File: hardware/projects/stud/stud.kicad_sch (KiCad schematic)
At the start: 1 part, among them U2 TAC5242

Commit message: add RA8M2, propose memory chip
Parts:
- added IC1: R7KA8M2JFLCAC#UC0, vendor:BGA289C65P17X17_1200X1200X138, symbol vendor:R7KA8M2JFLCAC#UC0
- added U1: IS42VM32160E-75BLI, vendor:TFBGA-90_8X13_ISI, symbol vendor:IS42VM32160E-75BLI
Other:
- moved on the sheet: U2

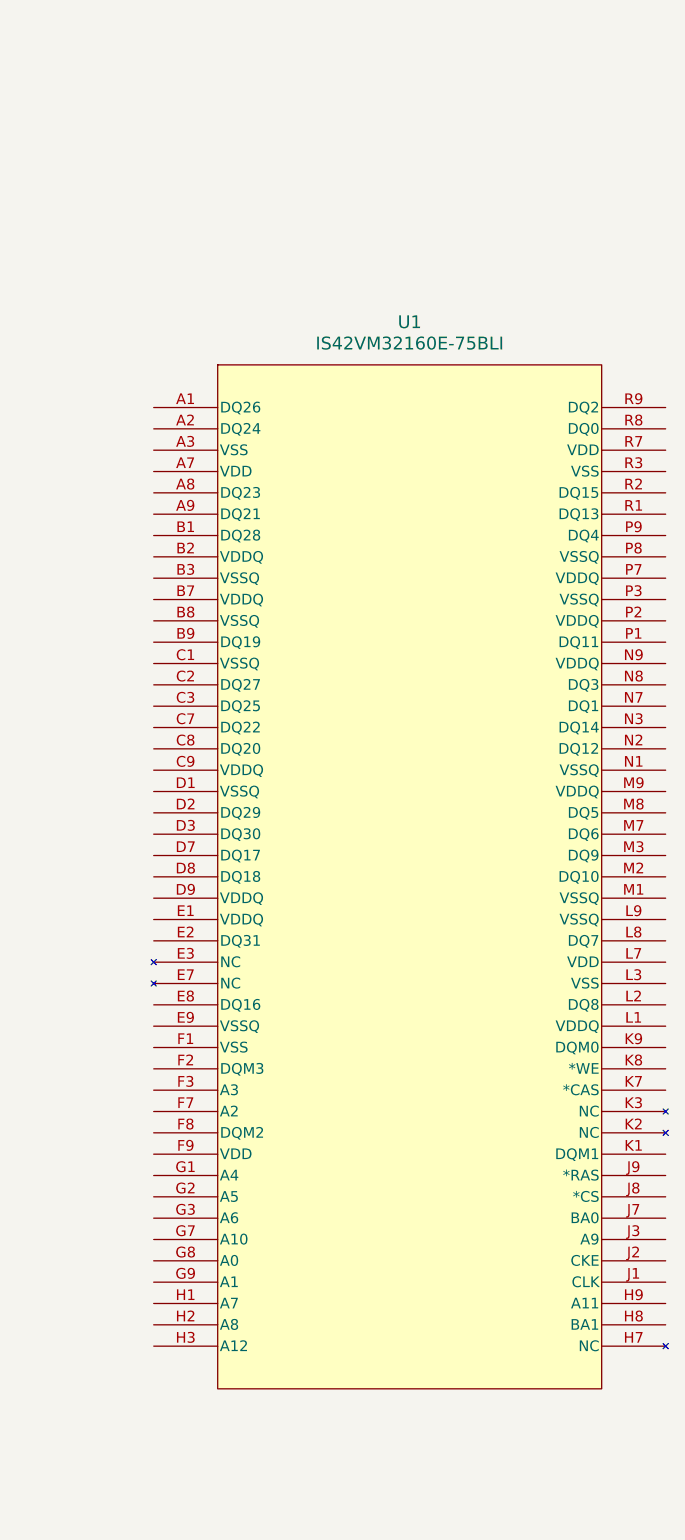
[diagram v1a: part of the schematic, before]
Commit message: switch SDRAM chips at fable's behest
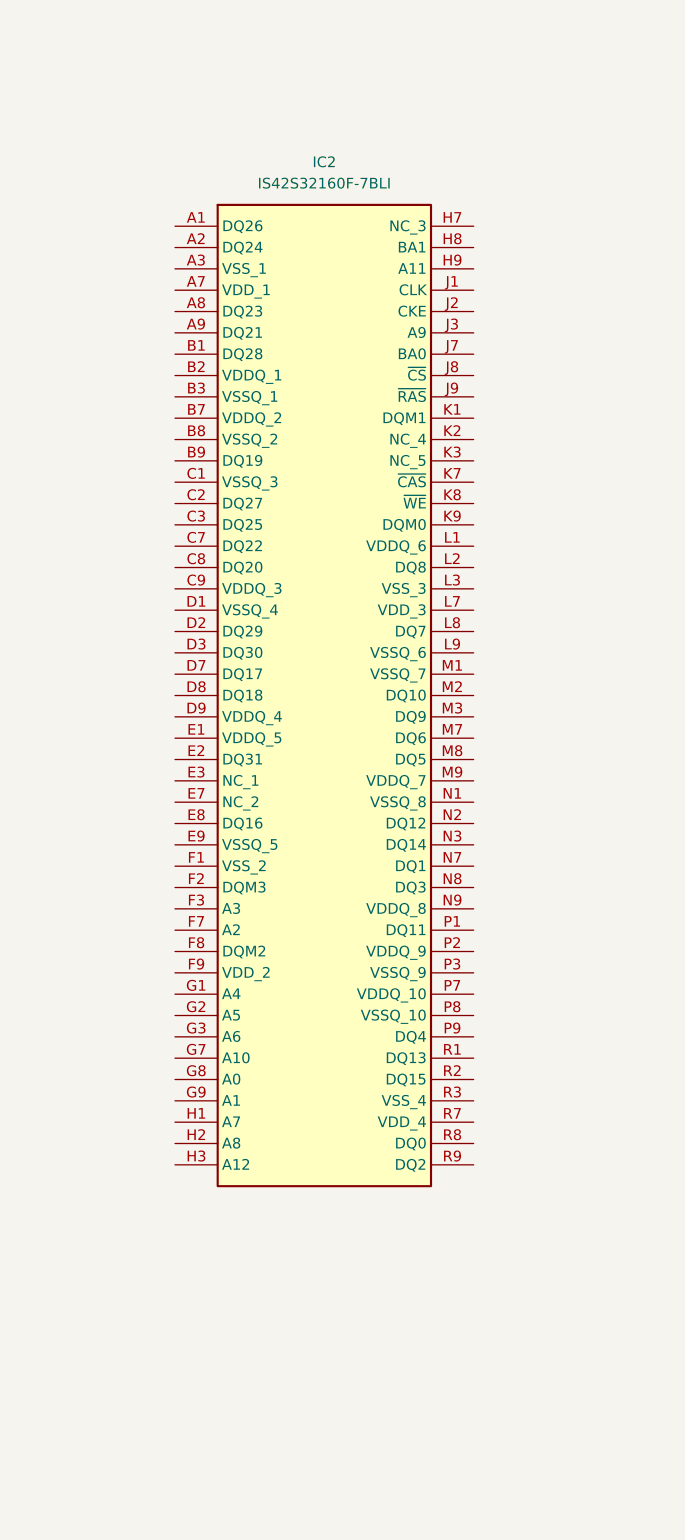
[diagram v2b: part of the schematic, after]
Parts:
- removed U1: IS42VM32160E-75BLI, vendor:TFBGA-90_8X13_ISI, symbol vendor:IS42VM32160E-75BLI
- added IC2: IS42S32160F-7BLI, vendor:BGA90C80P9X15_800X1300X120, symbol vendor:IS42S32160F-7BLI

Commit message: think about routing SDRAM traces
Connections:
- net DQ26: now reaches IC1.L3 (PC04)
- net DQ26: now also IC2.A1 (DQ26)
- net DQ21: now reaches IC1.L4 (PC09)
- net DQ21: now also IC2.A9 (DQ21)
- net DQ25: now reaches IC1.L5 (PC05)
- net DQ25: now also IC2.C3 (DQ25)
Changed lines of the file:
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@@
 		(company "stillmar electric")
+	)
+	(global_label "DQ26"
+		(shape bidirectional)
+		(at 184.15 184.15 180)
+		(fields_autoplaced yes)
+		(effects
+			(font
+				(size 1.27 1.27)
+			)
+			(justify right)
+		)
+		(property "Intersheetrefs" "${INTERSHEET_REFS}"
+			(at 175.034 184.15 0)
+			(hide yes)
+			(show_name no)
+			(do_not_autoplace no)
+			(effects
+				(font
+					(size 1.27 1.27)
+				)
+				(justify right)
+			)
+		)
+	)
+	(global_label "DQ25"
+		(shape bidirectional)
+		(at 107.95 167.64 0)
+		(fields_autoplaced yes)
+		(effects
+			(font
+				(size 1.27 1.27)
+			)
+			(justify left)
+		)
+		(property "Intersheetrefs" "${INTERSHEET_REFS}"
+			(at 117.066 167.64 0)
+			(hide yes)
+			(show_name no)
+			(do_not_autoplace no)
+			(effects
+				(font
+					(size 1.27 1.27)
+				)
+				(justify left)
+			)
+		)
+	)
+	(global_label "DQ25"
+		(shape bidirectional)
+		(at 184.15 219.71 180)
+		(fields_autoplaced yes)
+		(effects
+			(font
+				(size 1.27 1.27)
+			)
+			(justify right)
+		)
+		(property "Intersheetrefs" "${INTERSHEET_REFS}"
+			(at 175.034 219.71 0)
+			(hide yes)
+			(show_name no)
+			(do_not_autoplace no)
+			(effects
+				(font
+					(size 1.27 1.27)
+				)
+				(justify right)
+			)
+		)
+	)
+	(global_label "DQ26"
+		(shape bidirectional)
+		(at 107.95 162.56 0)
+		(fields_autoplaced yes)
+		(effects
+			(font
+				(size 1.27 1.27)
+			)
+			(justify left)
+		)
+		(property "Intersheetrefs" "${INTERSHEET_REFS}"
+			(at 117.066 162.56 0)
+			(hide yes)
+			(show_name no)
+			(do_not_autoplace no)
+			(effects
+				(font
+					(size 1.27 1.27)
+				)
+				(justify left)
+			)
+		)
+	)
+	(global_label "DQ21"
+		(shape bidirectional)
+		(at 184.15 196.85 180)
+		(fields_autoplaced yes)
+		(effects
+			(font
+				(size 1.27 1.27)
+			)
+			(justify right)
+		)
+		(property "Intersheetrefs" "${INTERSHEET_REFS}"
+			(at 175.034 196.85 0)
+			(hide yes)
+			(show_name no)
+			(do_not_autoplace no)
+			(effects
+				(font
+					(size 1.27 1.27)
+				)
+				(justify right)
+			)
+		)
+	)
+	(global_label "DQ21"
+		(shape bidirectional)
+		(at 107.95 165.1 0)
+		(fields_autoplaced yes)
+		(effects
+			(font
+				(size 1.27 1.27)
+			)
+			(justify left)
+		)
+		(property "Intersheetrefs" "${INTERSHEET_REFS}"
+			(at 117.066 165.1 0)
+			(hide yes)
+			(show_name no)
+			(do_not_autoplace no)
+			(effects
+				(font
+					(size 1.27 1.27)
+				)
+				(justify left)
+			)
+		)
 	)
 	(symbol

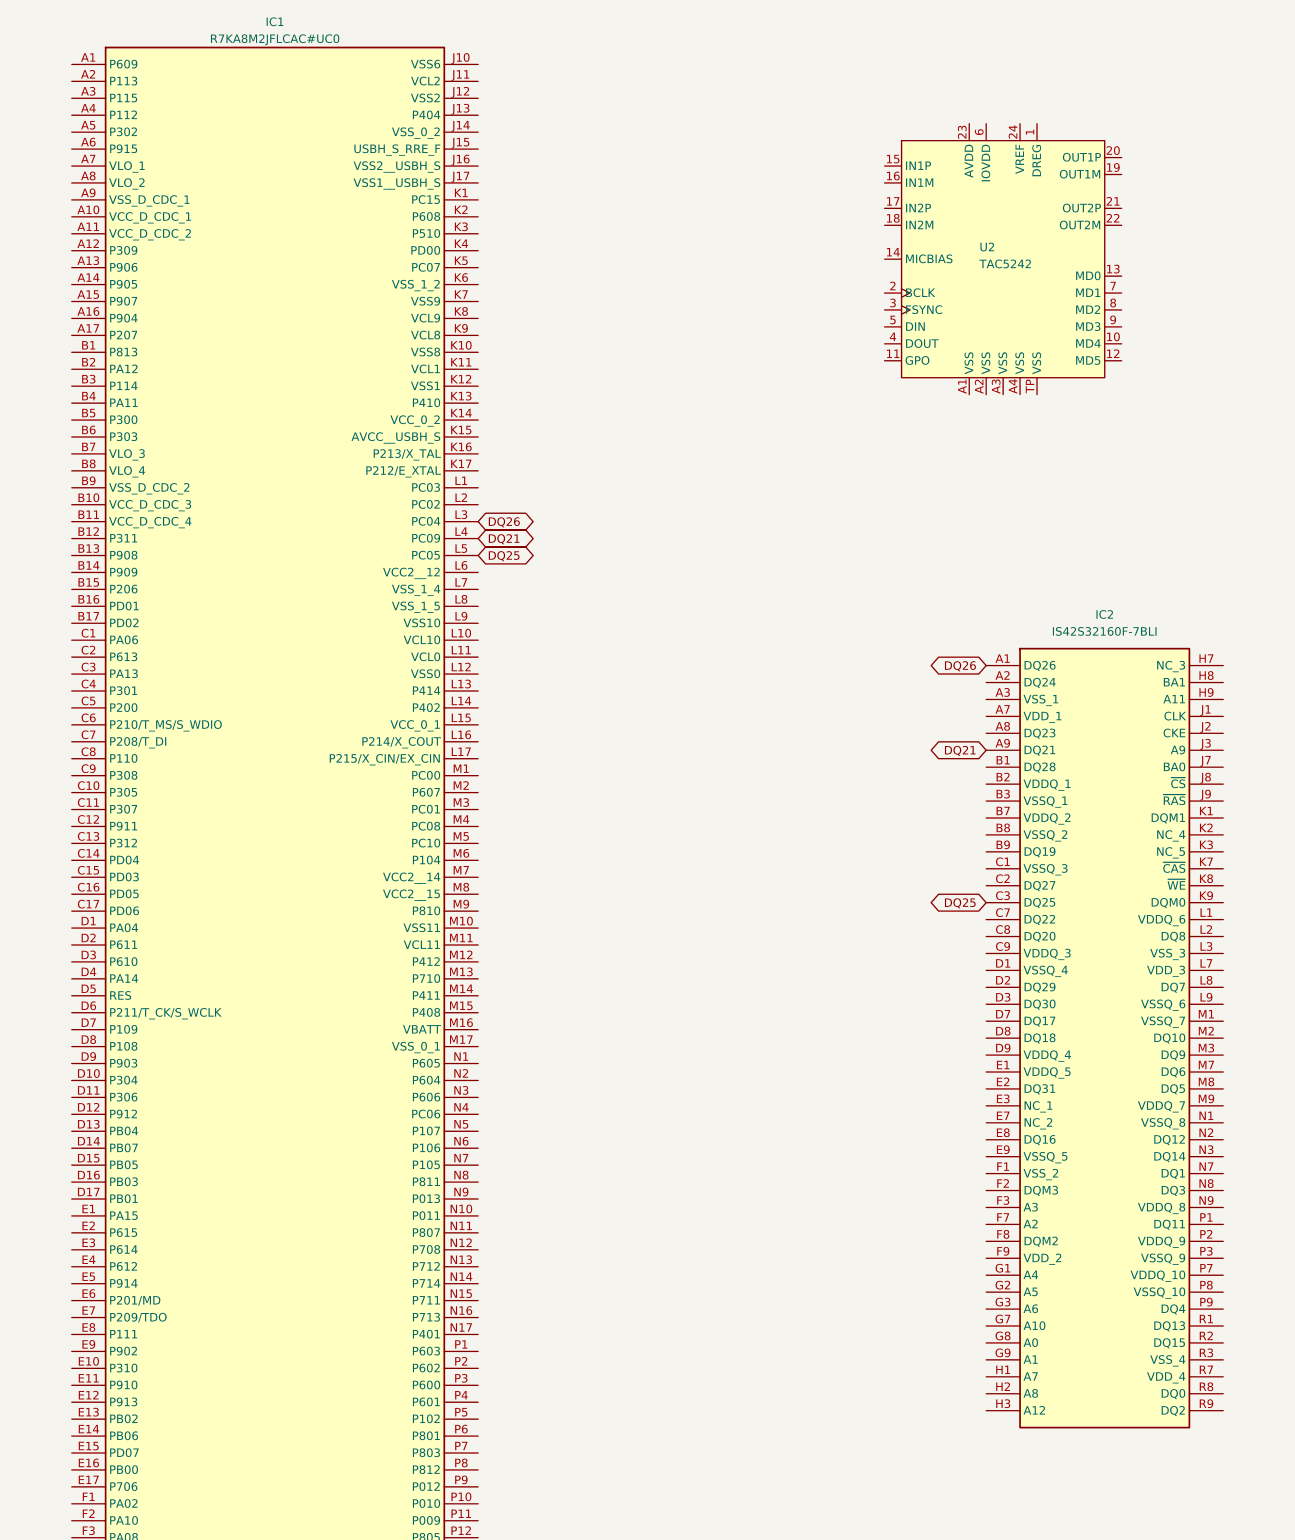
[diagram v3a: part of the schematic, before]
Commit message: add enough DQ nets to peek at connections
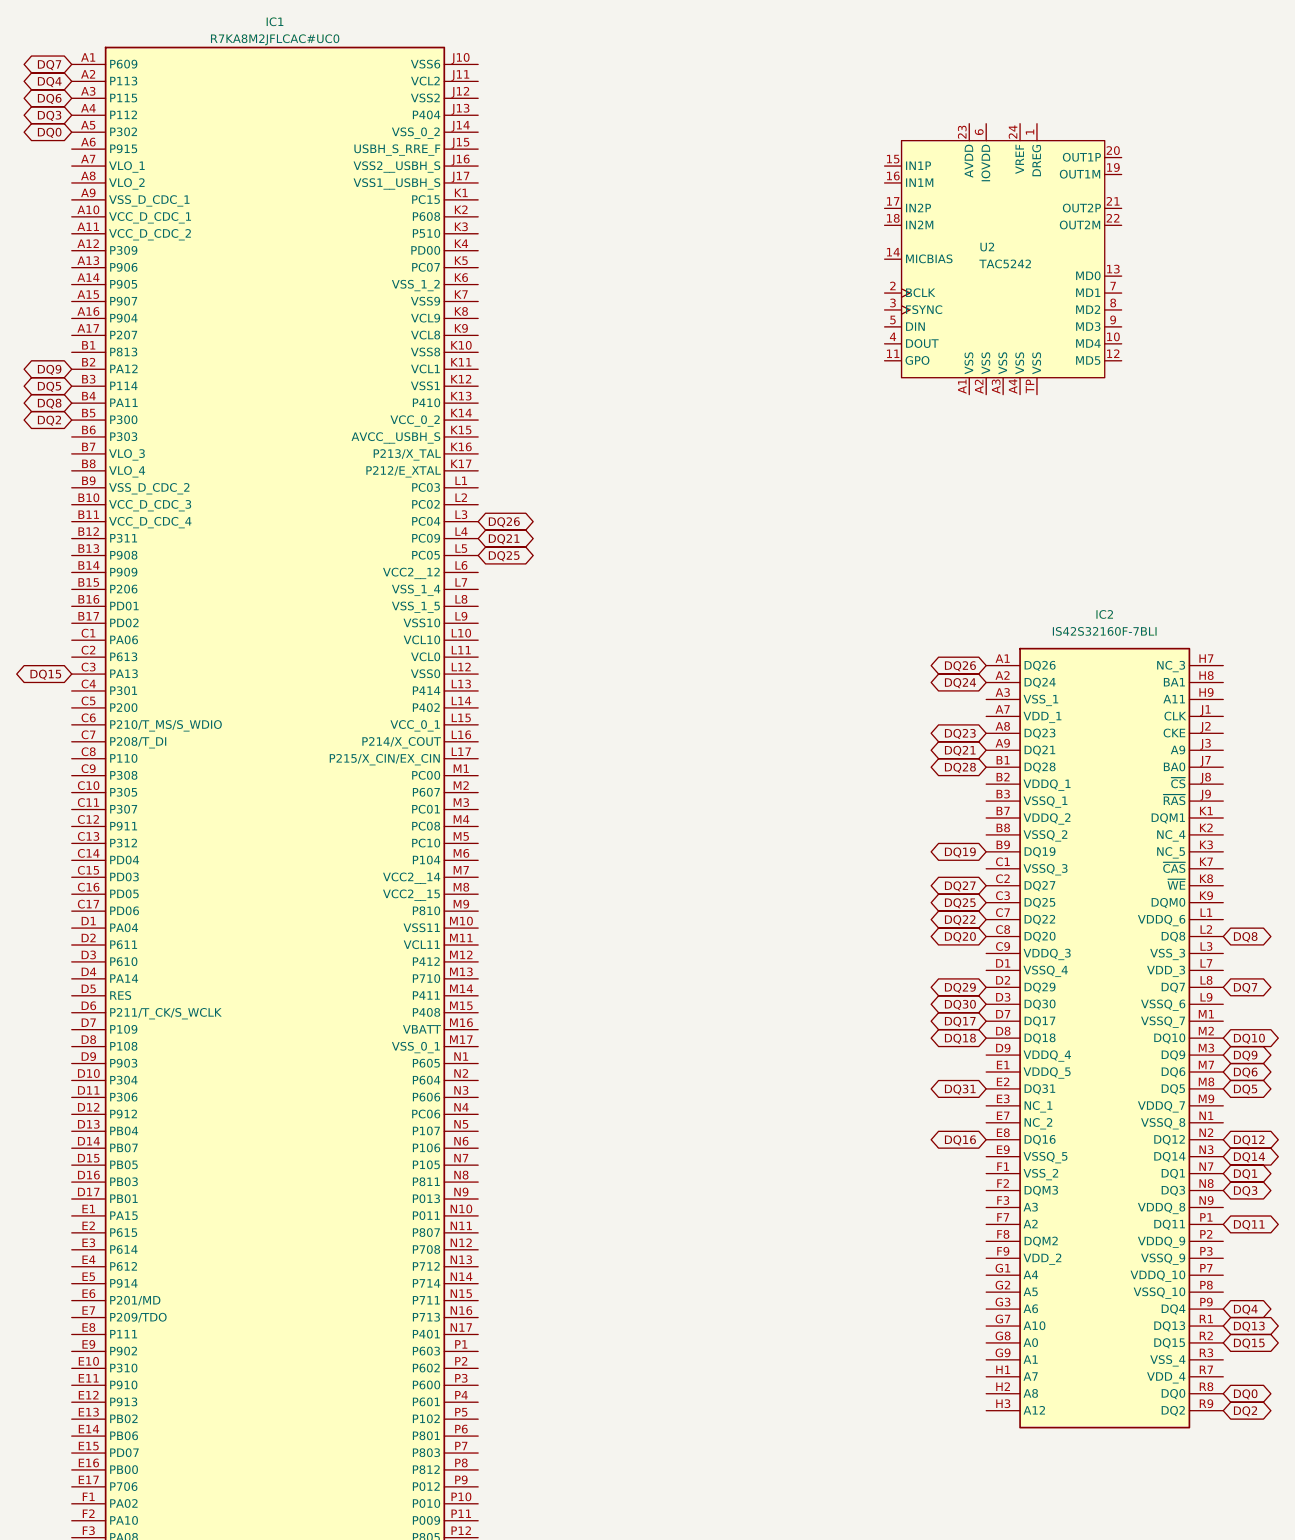
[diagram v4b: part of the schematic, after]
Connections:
- net DQ7: now reaches IC1.A1 (P609)
- net DQ7: now also IC2.L8 (DQ7)
- net DQ4: now reaches IC1.A2 (P113)
- net DQ4: now also IC2.P9 (DQ4)
- net DQ6: now reaches IC1.A3 (P115)
- net DQ6: now also IC2.M7 (DQ6)
- net DQ3: now reaches IC1.A4 (P112)
- net DQ3: now also IC2.N8 (DQ3)
- net DQ0: now reaches IC1.A5 (P302)
- net DQ0: now also IC2.R8 (DQ0)
- net DQ9: now reaches IC1.B2 (PA12)
- net DQ9: now also IC2.M3 (DQ9)
- net DQ5: now reaches IC1.B3 (P114)
- net DQ5: now also IC2.M8 (DQ5)
- net DQ8: now reaches IC1.B4 (PA11)
- net DQ8: now also IC2.L2 (DQ8)
- net DQ2: now reaches IC1.B5 (P300)
- net DQ2: now also IC2.R9 (DQ2)
- net DQ15: now reaches IC1.C3 (PA13)
- net DQ15: now also IC2.R2 (DQ15)
- net DQ24: now reaches IC2.A2 (DQ24)
- net DQ23: now reaches IC2.A8 (DQ23)
- net DQ28: now reaches IC2.B1 (DQ28)
- net DQ19: now reaches IC2.B9 (DQ19)
- net DQ27: now reaches IC2.C2 (DQ27)
- net DQ22: now reaches IC2.C7 (DQ22)
- net DQ20: now reaches IC2.C8 (DQ20)
- net DQ29: now reaches IC2.D2 (DQ29)
- net DQ30: now reaches IC2.D3 (DQ30)
- net DQ17: now reaches IC2.D7 (DQ17)
- net DQ18: now reaches IC2.D8 (DQ18)
- net DQ31: now reaches IC2.E2 (DQ31)
- net DQ16: now reaches IC2.E8 (DQ16)
- net DQ10: now reaches IC2.M2 (DQ10)
- net DQ12: now reaches IC2.N2 (DQ12)
- net DQ14: now reaches IC2.N3 (DQ14)
- net DQ1: now reaches IC2.N7 (DQ1)
- net DQ11: now reaches IC2.P1 (DQ11)
- net DQ13: now reaches IC2.R1 (DQ13)

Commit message: add a microSD connector
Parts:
- added MICRO_SD1: TF-01A, vendor:TF-01A, symbol vendor:TF-01A
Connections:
- new net SHIELD: MICRO_SD1.MP1 (SHIELD), MICRO_SD1.MP2 (SHIELD), MICRO_SD1.MP3 (SHIELD), MICRO_SD1.MP4 (SHIELD)
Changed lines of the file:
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@@
+	)
+	(symbol
+		(lib_id "vendor:TF-01A")
+		(at 247.65 119.38 0)
+		(unit 1)
+		(body_style 1)
+		(exclude_from_sim no)
+		(in_bom yes)
+		(on_board yes)
+		(in_pos_files yes)
+		(dnp no)
+		(fields_autoplaced yes)
+		(property "Reference" "MICRO_SD1"
+			(at 247.65 104.14 0)
+			(show_name no)
+			(do_not_autoplace no)
+			(effects
+				(font
+					(size 1.27 1.27)
+				)
+			)
+		)
+		(property "Value" "TF-01A"
+			(at 247.65 106.68 0)
+			(show_name no)
+			(do_not_autoplace no)
+			(effects
+				(font
+					(size 1.27 1.27)
+				)
+			)
+		)
+		(property "Footprint" "vendor:TF-01A"
+			(at 247.65 119.38 0)
+			(hide yes)
+			(show_name no)
+			(do_not_autoplace no)
+			(effects
+				(font
+					(size 1.27 1.27)
+				)
+				(justify bottom)
+			)
+		)
+		(property "Datasheet" ""
+			(at 247.65 119.38 0)
+			(hide yes)
+			(show_name no)
+			(do_not_autoplace no)
+			(effects
+				(font
+					(size 1.27 1.27)
+				)
+			)
+		)
+		(property "Description" "Standard Card Edge Connectors"
+			(at 247.65 119.38 0)
+			(hide yes)
+			(show_name no)
+			(do_not_autoplace no)
+			(effects
+				(font
+					(size 1.27 1.27)
+				)
+				(justify bottom)
+			)
+		)
+		(property "MF" "HRO Electronics Co., Ltd."
+			(at 247.65 119.38 0)
+			(hide yes)
+			(show_name no)
+			(do_not_autoplace no)
+			(effects
+				(font
+					(size 1.27 1.27)
+				)
+				(justify bottom)
+			)
+		)
+		(property "Package" "Package"
+			(at 247.65 119.38 0)
+			(hide yes)
+			(show_name no)
+			(do_not_autoplace no)
+			(effects
+				(font
+					(size 1.27 1.27)
+				)
+				(justify bottom)
+			)
+		)
+		(property "Price" "None"
+			(at 247.65 119.38 0)
+			(hide yes)
+			(show_name no)
+			(do_not_autoplace no)
+			(effects
+				(font
+					(size 1.27 1.27)
+				)
+				(justify bottom)
+			)
+		)
+		(property "SnapEDA_Link" "https://www.snapeda.com/parts/TF-01A/HRO+Electronics+Co.%252C+Ltd./view-part/?ref=snap"
+			(at 247.65 119.38 0)
+			(hide yes)
+			(show_name no)
+			(do_not_autoplace no)
+			(effects
+				(font
+					(size 1.27 1.27)
+				)
+				(justify bottom)
+			)
+		)
+		(property "MP" "TF-01A"
+			(at 247.65 119.38 0)
+			(hide yes)
+			(show_name no)
+			(do_not_autoplace no)
+			(effects
+				(font
+					(size 1.27 1.27)
+				)
+				(justify bottom)
+			)
+		)
+		(property "Availability" "In Stock"
+			(at 247.65 119.38 0)
+			(hide yes)
+			(show_name no)
+			(do_not_autoplace no)
+			(effects
+				(font
+					(size 1.27 1.27)
+				)
+				(justify bottom)
+			)
+		)
+		(property "Check_prices" "https://www.snapeda.com/parts/TF-01A/HRO+Electronics+Co.%252C+Ltd./view-part/?ref=eda"
+			(at 247.65 119.38 0)
+			(hide yes)
+			(show_name no)
+			(do_not_autoplace no)
+			(effects
+				(font
+					(size 1.27 1.27)
+				)
+				(justify bottom)
+			)
+		)
+		(pin "8"
+		)
+		(pin "2"
+		)
+		(pin "1"
+		)
+		(pin "3"
+		)
+		(pin "4"
+		)
+		(pin "5"
+		)
+		(pin "CD1"
+		)
+		(pin "6"
+		)
+		(pin "MP4"
+		)
+		(pin "MP3"
+		)
+		(pin "7"
+		)
+		(pin "MP2"
+		)
+		(pin "MP1"
+		)
+		(instances
+			(project "stud"
+				(path "/5a440a9e-b660-4605-bd2b-6a991cc5b149"
+					(reference "MICRO_SD1")
+					(unit 1)
+				)
+			)
+		)
 	)
 	(symbol
